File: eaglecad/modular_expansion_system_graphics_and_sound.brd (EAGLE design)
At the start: 90.2 x 100 mm, 55 parts, among them IC1 74LS244N, IC2 ATF22V10, IC3 74LS74N, IC8 74LS244N, IC9-74HCU04 74LS04N, J1-INTERRUPTS INTERRUPTS, J1_ADDRESS_CON j1, J2-WAITS WAITS, J2_DATA_AND_POWER_CON j2, J3-VIDEO-OUT RCA, J4-AUDIO-LEFT RCA, J5-AUDIO-RIGHT RCA, Q2 2N2222, U1 TMS4416, U11 SN76489, U2 TMS9118, U3 TMS4416, U4 SN76489, U5 SN76489, U6 SN76489, Y1 OSC1-CPP-4

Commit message: updated readme and minor updates to schematic for gs board
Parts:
- renumbered IC1 to IC1_JOY2_BUF, IC2 to IC2_GLU, IC8 to IC8_JOY1_BUF, U1 to U1_TMS_RAM, U11 to U11_SND1, U2 to U2_VDP, U3 to U3_TMS_RAM, U4 to U4_SND2, U5 to U5_SND3, U6 to U6_SND4
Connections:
- net N$11 renamed SND4_ENABLE_N
- net N$15 renamed SND4_READY
- net N$8 renamed SND3_READY
- net N$9 renamed SND3_ENABLE_N

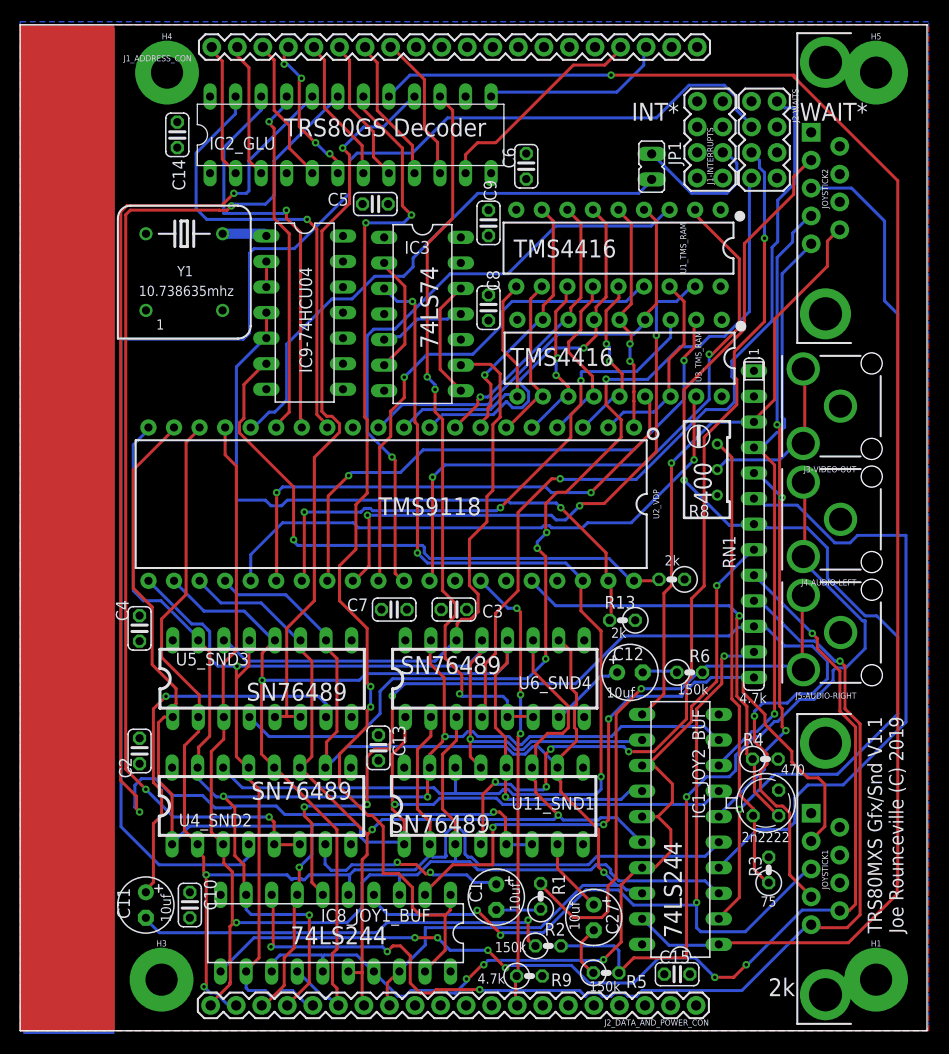
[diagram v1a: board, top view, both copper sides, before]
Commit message: added inductor to grfx brd and removed extra 7805
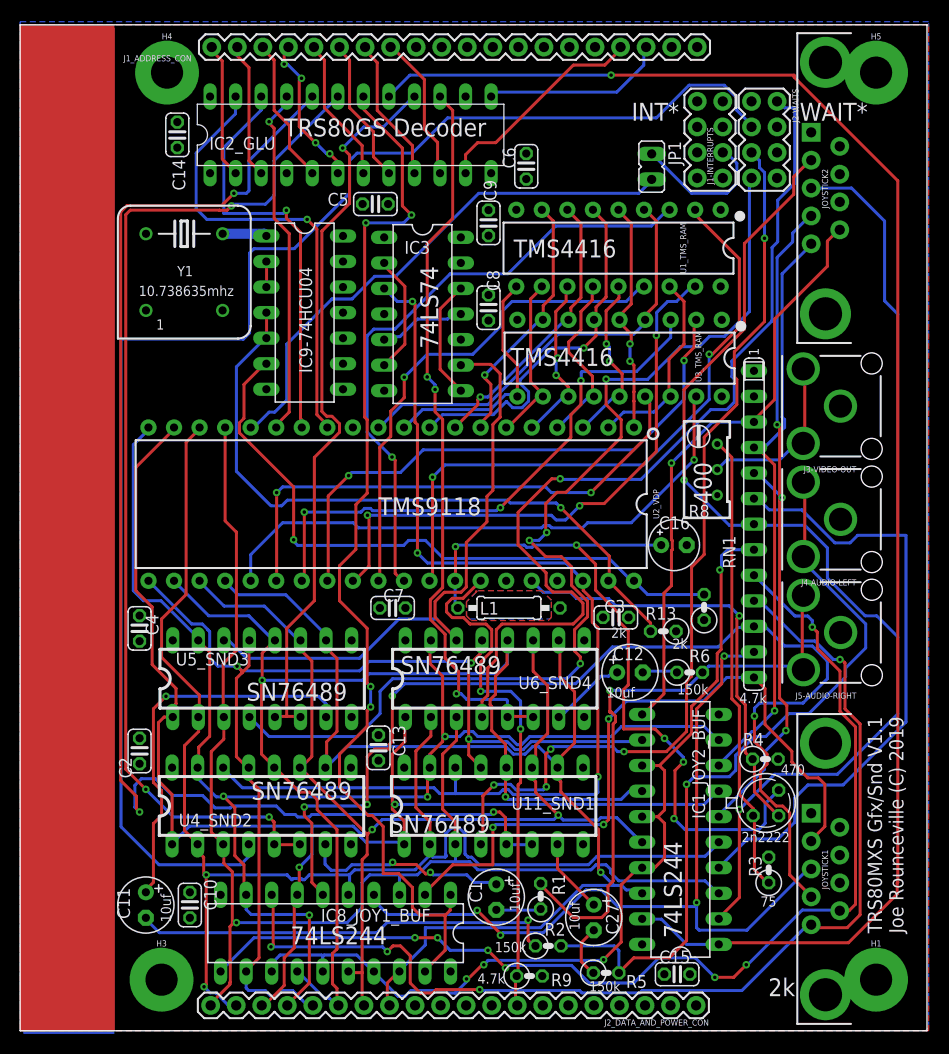
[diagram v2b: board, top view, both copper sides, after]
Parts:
- added C16: 22uF, resistor:E2,5-5
- added L1: 6.8uH, eagle-ltspice:0207/10
- moved C3 16.1 mm to (59.2, 41.1), turned to 0 degrees
- moved R12 4.25 mm to (68.0, 42.1), turned to 90 degrees
- moved R13 4.21 mm to (63.9, 39.7)
- moved C7 0.22 mm to (37.0, 42.0)
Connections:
- new net VID-VCC: C16.+, L1.1, Q2.C, U2_VDP.P33
- net GND: now also C16.-
- net VCC: now also L1.2; no longer Q2.C, U2_VDP.P33
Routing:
- net VID-VCC: track 0.00 -> 74.8 mm, vias 0 -> 5
- net SND4_READY: track 82.0 -> 92.6 mm
- net SND3_READY: track 98.2 -> 106.5 mm
- net SYSRES*: track 44.6 -> 51.8 mm, vias 3 -> 2
- net CLK-IN-1: track 59.4 -> 64.5 mm
- net CLOCK_DIV_4: track 58.7 -> 61.8 mm
- net D6: track 106.0 -> 103.5 mm
- net D4: track 117.1 -> 115.0 mm, vias 2 -> 3
- net N$24: track 56.9 -> 59.0 mm
- net UP: track 71.7 -> 70.2 mm
- net D2: track 139.2 -> 138.0 mm
- net D5: track 116.4 -> 117.4 mm
- net CLK-IN-2: track 66.4 -> 67.3 mm
- net TRIGGER: track 108.4 -> 109.1 mm
- net VDP-RD3: track 58.5 -> 57.8 mm
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- added copper zone on layer 16, net GND
- added copper zone on layer 1, net VCC

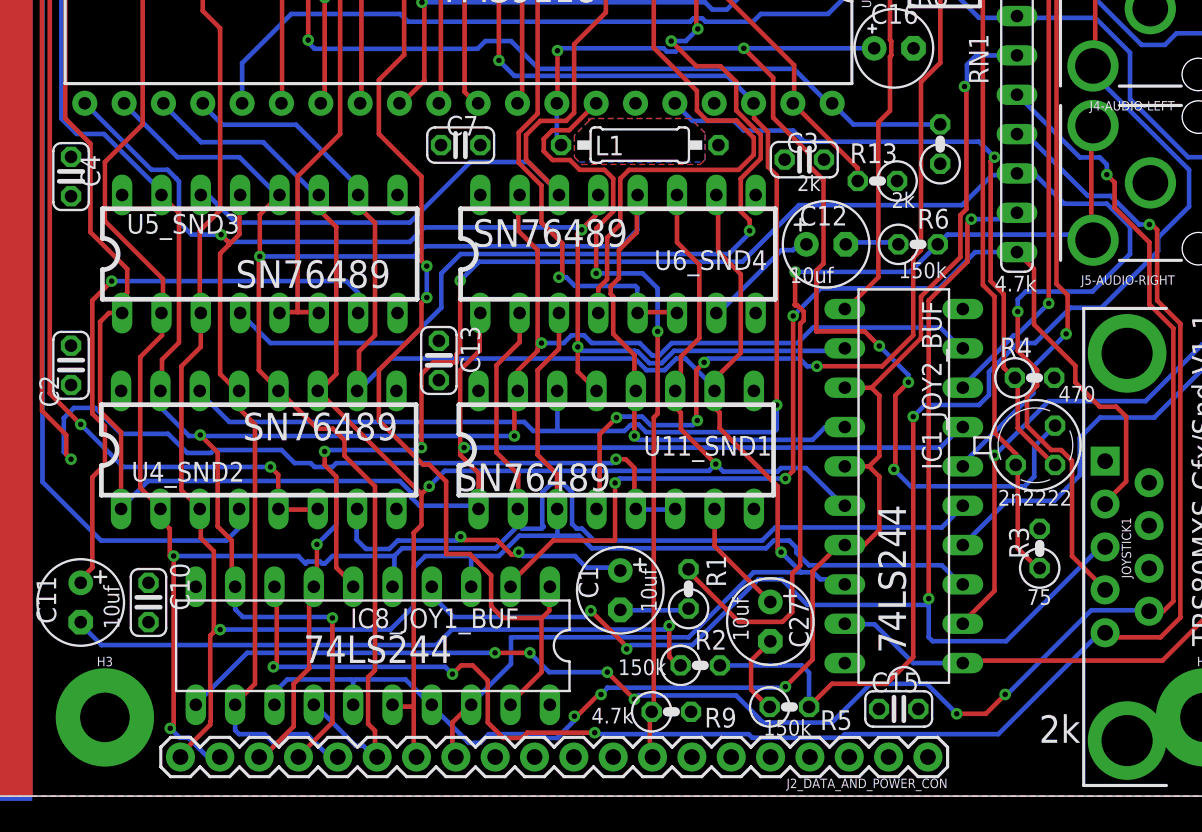
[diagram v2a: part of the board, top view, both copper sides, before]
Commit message: fixed WRITE code in drive emulation and added music stuff
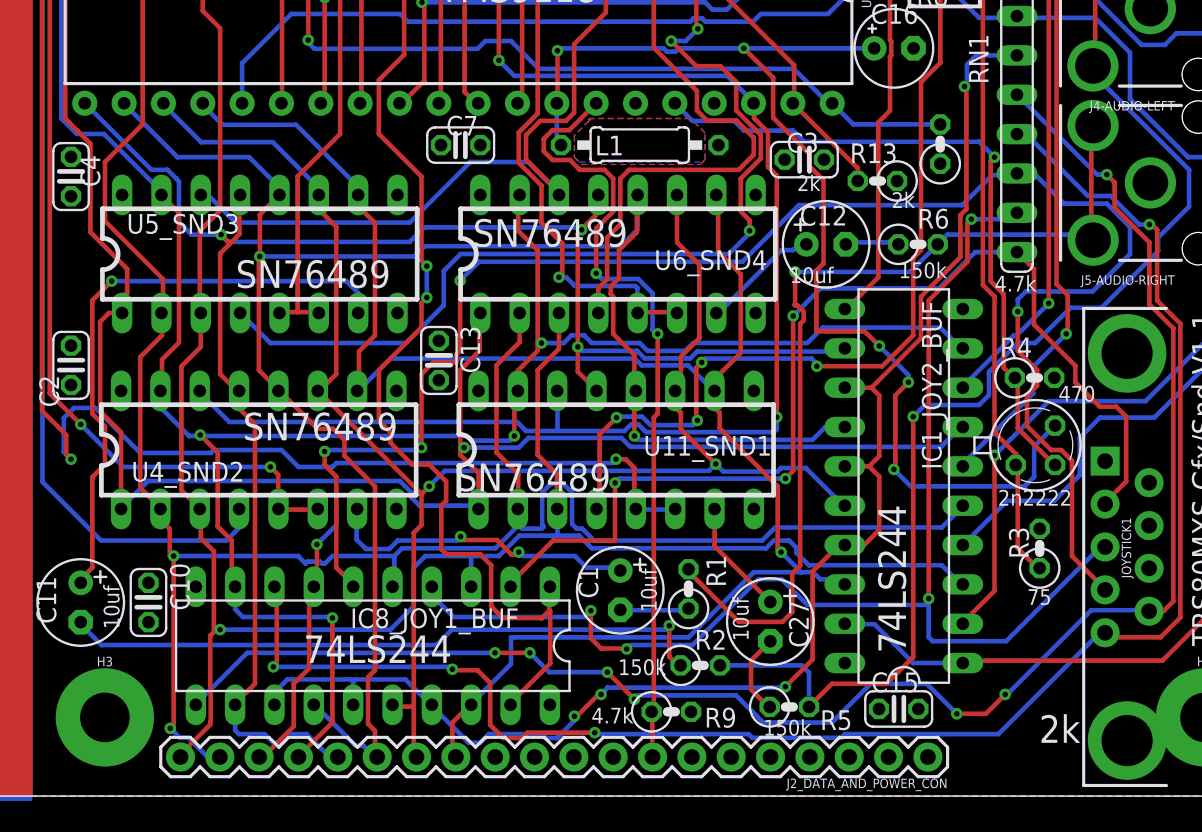
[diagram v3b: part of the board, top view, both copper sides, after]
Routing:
- net JOY1_IN_ENABLE_N: track 106.9 -> 108.8 mm
- net DOWN: track 82.3 -> 83.3 mm
- net D7: track 113.0 -> 112.3 mm

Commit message: updated schematics, boards, and pdfs
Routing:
- net N$1: track 75.8 -> 77.6 mm
- net LEFT: track 108.3 -> 109.5 mm
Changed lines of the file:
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@@
 <wire x1="73" y1="28.75" x2="74.25" y2="27.5" width="0.3" layer="1"/>
 <wire x1="73" y1="31.28125" x2="73" y2="28.75" width="0.3" layer="1"/>
-<wire x1="73.515625" y1="32.578125" x2="73" y2="32.0625" width="0.3" layer="16"/>
+<wire x1="73.828125" y1="32.890625" x2="73" y2="32.0625" width="0.3" layer="16"/>
 <wire x1="73" y1="32.0625" x2="73" y2="31.28125" width="0.3" layer="16"/>
-<wire x1="80.25" y1="36.75" x2="80.25" y2="35" width="0.3" layer="16"/>
+<wire x1="80.25" y1="36.75" x2="80.25" y2="32.96875" width="0.3" layer="16"/>
 <wire x1="78.75" y1="38.25" x2="80.25" y2="36.75" width="0.3" layer="16"/>
 <wire x1="76" y1="38.25" x2="78.75" y2="38.25" width="0.3" layer="16"/>
@@
 <wire x1="75.80880625" y1="22.3428" x2="76.5" y2="21.65160625" width="0.3" layer="1"/>
 <wire x1="76.5" y1="21.65160625" x2="76.5" y2="15.5" width="0.3" layer="1"/>
-<wire x1="80.25" y1="35" x2="77.828125" y2="32.578125" width="0.3" layer="16"/>
-<wire x1="77.828125" y1="32.578125" x2="73.515625" y2="32.578125" width="0.3" layer="16"/>
+<wire x1="80.25" y1="32.96875" x2="80.171875" y2="32.890625" width="0.3" layer="16"/>
+<wire x1="80.171875" y1="32.890625" x2="73.828125" y2="32.890625" width="0.3" layer="16"/>
 <wire x1="28.25" y1="22.25" x2="28.25" y2="21.375" width="0.3" layer="1"/>
 <wire x1="28.25" y1="21.375" x2="29" y2="20.625" width="0.3" layer="1"/>
@@
 <wire x1="59.525" y1="7.975" x2="59.0625" y2="8.4375" width="0.3" layer="16"/>
 <wire x1="59.0625" y1="8.4375" x2="53.77" y2="8.4375" width="0.3" layer="16"/>
-<wire x1="74.125" y1="29.25" x2="76.40625" y2="31.53125" width="0.3" layer="16"/>
+<wire x1="74.125" y1="29.25" x2="76.875" y2="32" width="0.3" layer="16"/>
 <wire x1="71.140625" y1="25.890625" x2="71.140625" y2="27.390625" width="0.3" layer="16"/>
 <wire x1="71.140625" y1="27.390625" x2="73" y2="29.25" width="0.3" layer="16"/>
-<wire x1="82.0625" y1="36.0625" x2="82.0625" y2="35.1875" width="0.3" layer="16"/>
-<wire x1="76.40625" y1="31.53125" x2="78.40625" y2="31.53125" width="0.3" layer="16"/>
-<wire x1="78.40625" y1="31.53125" x2="82.0625" y2="35.1875" width="0.3" layer="16"/>
 <wire x1="78" y1="46.5" x2="84.0625" y2="40.4375" width="0.3" layer="16"/>
 <wire x1="84.0625" y1="40.4375" x2="84.0625" y2="38.0625" width="0.3" layer="16"/>
-<wire x1="84.0625" y1="38.0625" x2="82.0625" y2="36.0625" width="0.3" layer="16"/>
+<wire x1="82.0625" y1="36.0625" x2="84.0625" y2="38.0625" width="0.3" layer="16"/>
 <wire x1="66.25" y1="24.5" x2="66.25" y2="8.96875" width="0.3" layer="1"/>
 <wire x1="66.25" y1="8.96875" x2="64.53125" y2="7.25" width="0.3" layer="1"/>
+<wire x1="76.875" y1="32" x2="82" y2="32" width="0.3" layer="16"/>
+<wire x1="82" y1="32" x2="82.0625" y2="32.0625" width="0.3" layer="16"/>
+<wire x1="82.0625" y1="32.0625" x2="82.0625" y2="36.0625" width="0.3" layer="16"/>
 </signal>
 <signal name="SND1_READY">

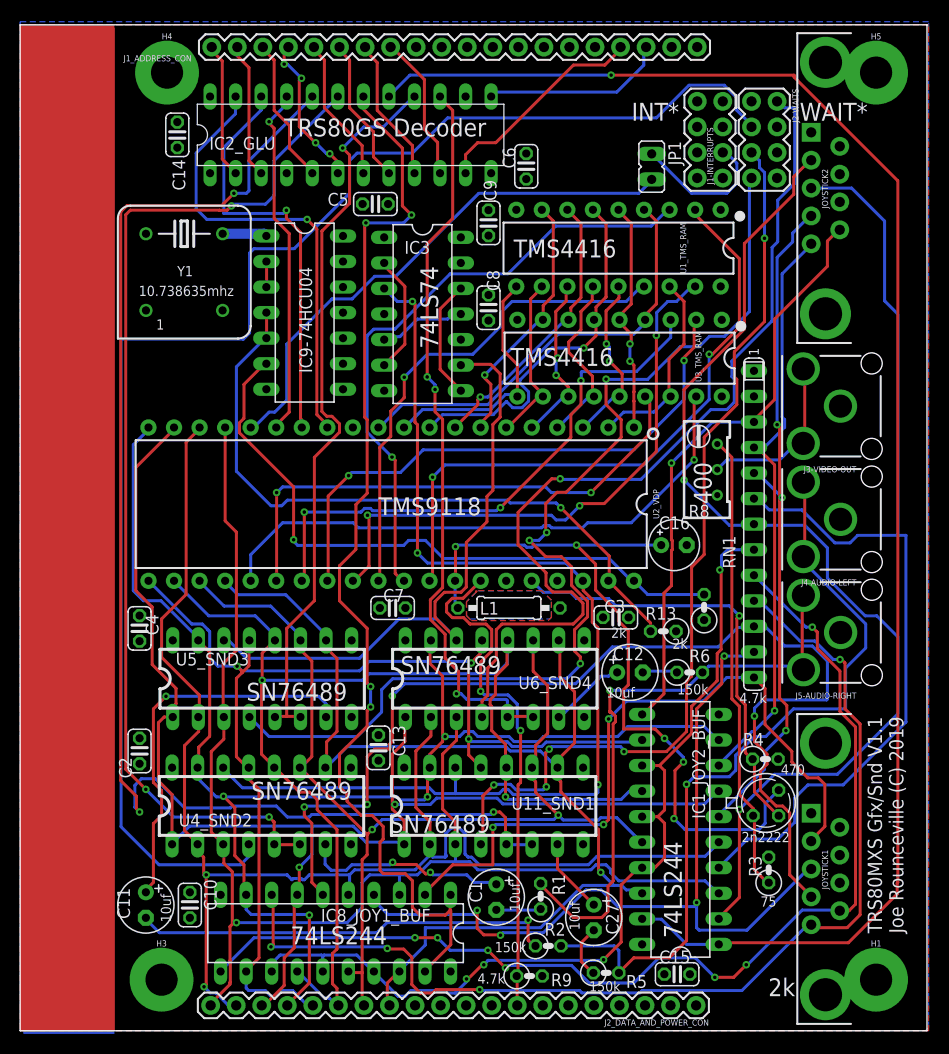
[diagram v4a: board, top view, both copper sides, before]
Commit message: implemented pacman fruit behavior
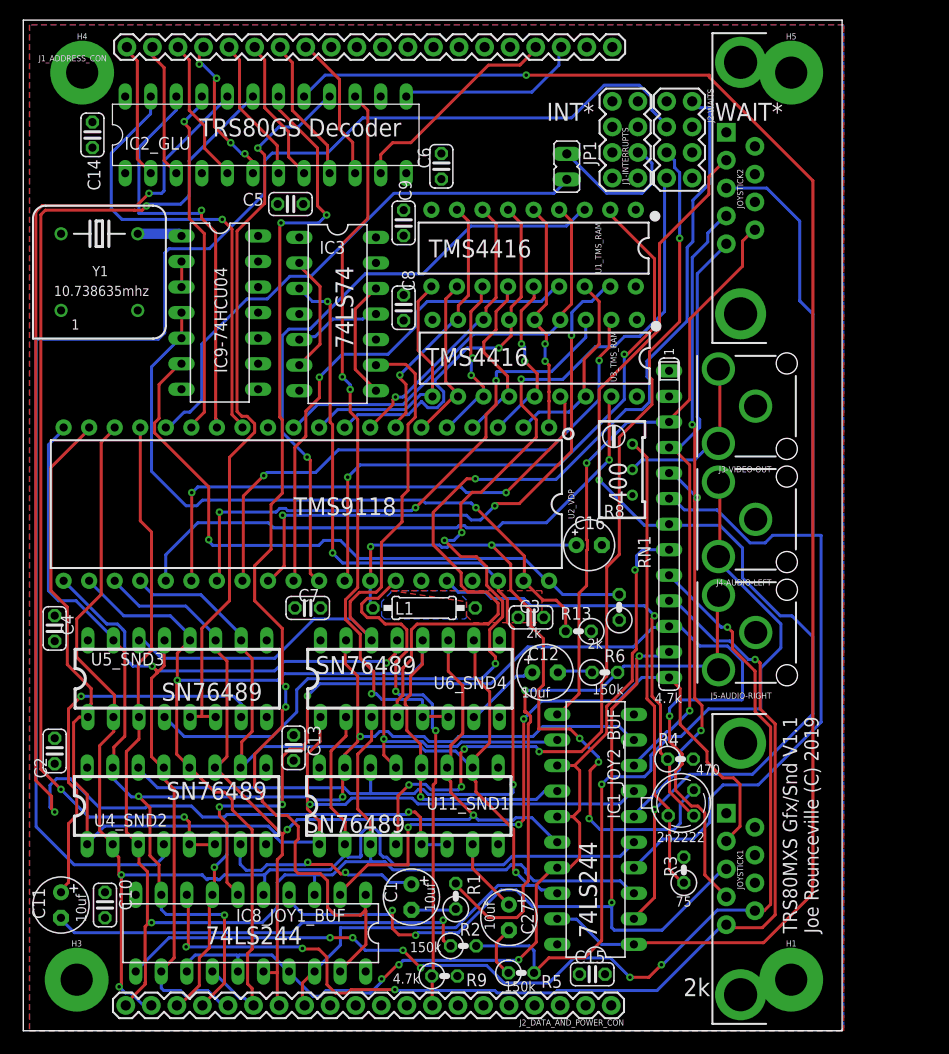
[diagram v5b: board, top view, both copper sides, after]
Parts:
- moved R12 8.44 mm to (59.6, 42.1)
- moved U4_SND2 8.44 mm to (15.6, 22.4)
- moved C1 8.44 mm to (38.9, 13.3)
- moved C10 8.44 mm to (8.44, 12.5)
- moved C11 8.44 mm to (4.06, 12.5)
- moved C12 8.44 mm to (52.2, 35.6)
- moved C13 8.44 mm to (27.2, 28.1)
- moved C14 8.44 mm to (7.19, 89.1)
- moved C15 8.44 mm to (56.9, 5.62)
- moved C16 8.44 mm to (56.6, 48.3)
- moved C2 8.44 mm to (3.44, 27.8)
- moved C27 8.44 mm to (48.6, 11.3)
- moved C3 8.44 mm to (50.8, 41.1)
- moved C4 8.44 mm to (3.44, 40.0)
- moved C5 8.44 mm to (26.9, 82.2)
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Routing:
- net CLK-IN-2: track 67.3 -> 68.1 mm
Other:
- board size 90.2 x 100 mm -> 81.4 x 100.5 mm

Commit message: tweaked graphics card to match older TRS80 joysticks and tweaked pacman game
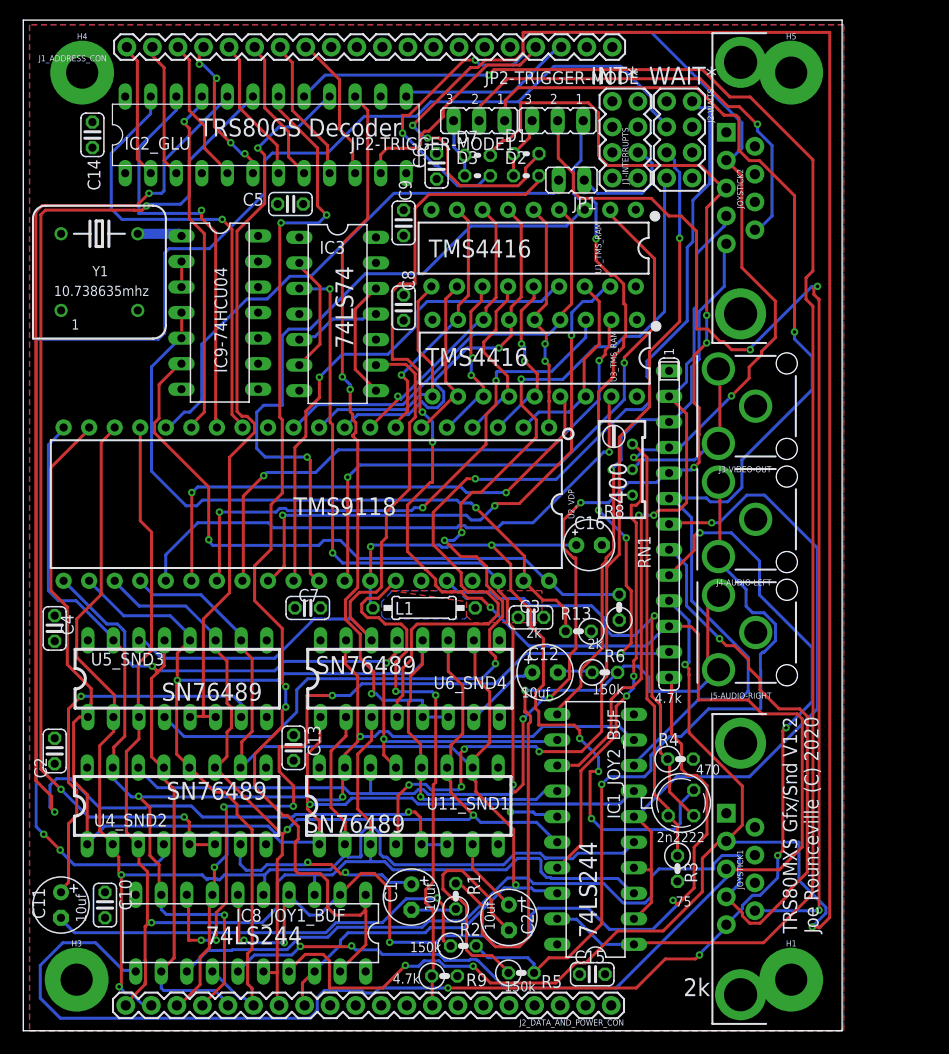
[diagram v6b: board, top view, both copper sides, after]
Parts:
- added D1, D2, D3, D7: (1N821), rcl:0204V
- added JP2-TRIGGER-MODE, JP2-TRIGGER-MODE1: (no value), jumper:JP2
- moved JP1 1.42 mm to (54.8, 84.6), turned to 90 degrees
- moved R3 0.64 mm to (65.3, 16.1), turned to 270 degrees
- moved C6 0.47 mm to (41.4, 85.9)
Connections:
- removed net N$99: IC1_JOY2_BUF.13, IC1_JOY2_BUF.15, IC1_JOY2_BUF.17, IC8_JOY1_BUF.13, IC8_JOY1_BUF.15, IC8_JOY1_BUF.17, RN1.8
- new net 5_BIT_TRIGGER_LINE: IC8_JOY1_BUF.8, JP2-TRIGGER-MODE.1, RN1.12
- new net 5_BIT_TRIGGER_LINE_2: IC1_JOY2_BUF.8, JP2-TRIGGER-MODE1.1, RN1.6
- new net N$11: IC8_JOY1_BUF.2, IC8_JOY1_BUF.4, IC8_JOY1_BUF.6, RN1.13
- new net N$20: IC1_JOY2_BUF.2, IC1_JOY2_BUF.4, IC1_JOY2_BUF.6, RN1.7
- new net TOPOFDIODES: D1.1, D2.1, JP2-TRIGGER-MODE.3
- new net TOPOFDIODES1: D3.1, D7.1, JP2-TRIGGER-MODE1.3
- net DOWN: now also D2.2, IC8_JOY1_BUF.15, RN1.11; no longer IC8_JOY1_BUF.4, RN1.12
- net DOWN1: now also D7.2, IC1_JOY2_BUF.15, RN1.5; no longer IC1_JOY2_BUF.4, RN1.6
- net LEFT: now also IC8_JOY1_BUF.13, RN1.8; no longer IC8_JOY1_BUF.6, RN1.11
- net LEFT1: now also IC1_JOY2_BUF.13, RN1.2; no longer IC1_JOY2_BUF.6, RN1.5
- net RIGHT: now also IC8_JOY1_BUF.11, RN1.9; no longer IC8_JOY1_BUF.8, RN1.10
- net RIGHT1: now also IC1_JOY2_BUF.11, RN1.3; no longer IC1_JOY2_BUF.8, RN1.4
- net TRIGGER: now also JP2-TRIGGER-MODE.2; no longer IC8_JOY1_BUF.11, RN1.9
- net TRIGGER1: now also JP2-TRIGGER-MODE1.2; no longer IC1_JOY2_BUF.11, RN1.3
- net UP: now also D1.2, IC8_JOY1_BUF.17, RN1.10; no longer IC8_JOY1_BUF.2, RN1.13
- net UP1: now also D3.2, IC1_JOY2_BUF.17, RN1.4; no longer IC1_JOY2_BUF.2, RN1.7
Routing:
- net UP: track 70.2 -> 257.7 mm, vias 3 -> 6
- net 5_BIT_TRIGGER_LINE: track 0.00 -> 139.8 mm, vias 0 -> 9
- net 5_BIT_TRIGGER_LINE_2: track 0.00 -> 115.2 mm, vias 0 -> 1
- net DOWN: track 83.3 -> 184.1 mm, vias 4 -> 5
- net N$11: track 0.00 -> 94.0 mm, vias 0 -> 4
- net N$99: track 93.2 -> 0.00 mm, vias 4 -> 0
- net N$20: track 0.00 -> 70.3 mm, vias 0 -> 1
- net UP1: track 105.7 -> 145.1 mm, vias 2 -> 6
- net RIGHT: track 108.5 -> 144.0 mm, vias 4 -> 5
- net N$64: track 5.30 -> 24.0 mm
- net TRIGGER1: track 58.9 -> 44.2 mm
- net DOWN1: track 102.3 -> 115.9 mm, vias 0 -> 7
- net LEFT: track 109.5 -> 119.0 mm, vias 4 -> 1
- net N$24: track 59.0 -> 68.1 mm
- net TRIGGER: track 108.7 -> 115.7 mm, vias 7 -> 3
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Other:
- board text added: "TRS80MXS Gfx/Snd V1.2 Joe Rounceville (C) 2020"
- board text removed: "TRS80MXS Gfx/Snd V1.1 Joe Rounceville (C) 2019"
